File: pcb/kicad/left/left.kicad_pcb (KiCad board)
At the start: 2 copper layers, 135.9 x 89.5 mm, 61 parts, among them J1 USB_C_Receptacle_USB2.0, J2 AudioJack4, J3 Conn_01x12_Male, SW1 BOOT, SW10 SW_Push, SW12 SW_Push, SW13 SW_Push, SW14 SW_Push, SW15 SW_Push, SW17 SW_Push, SW18 SW_Push, SW19 SW_Push, SW2 RESET, SW21 SW_Push, SW22 SW_Push, SW23 SW_Push, SW24 SW_Push, SW3 SW_Push, SW31 SW_Push, SW32 SW_Push, SW33 SW_Push, SW34 SW_Push, SW4 SW_Push, SW5 SW_Push, SW7 SW_Push, SW8 SW_Push, SW9 SW_Push, U1 STM32, U2 LDO

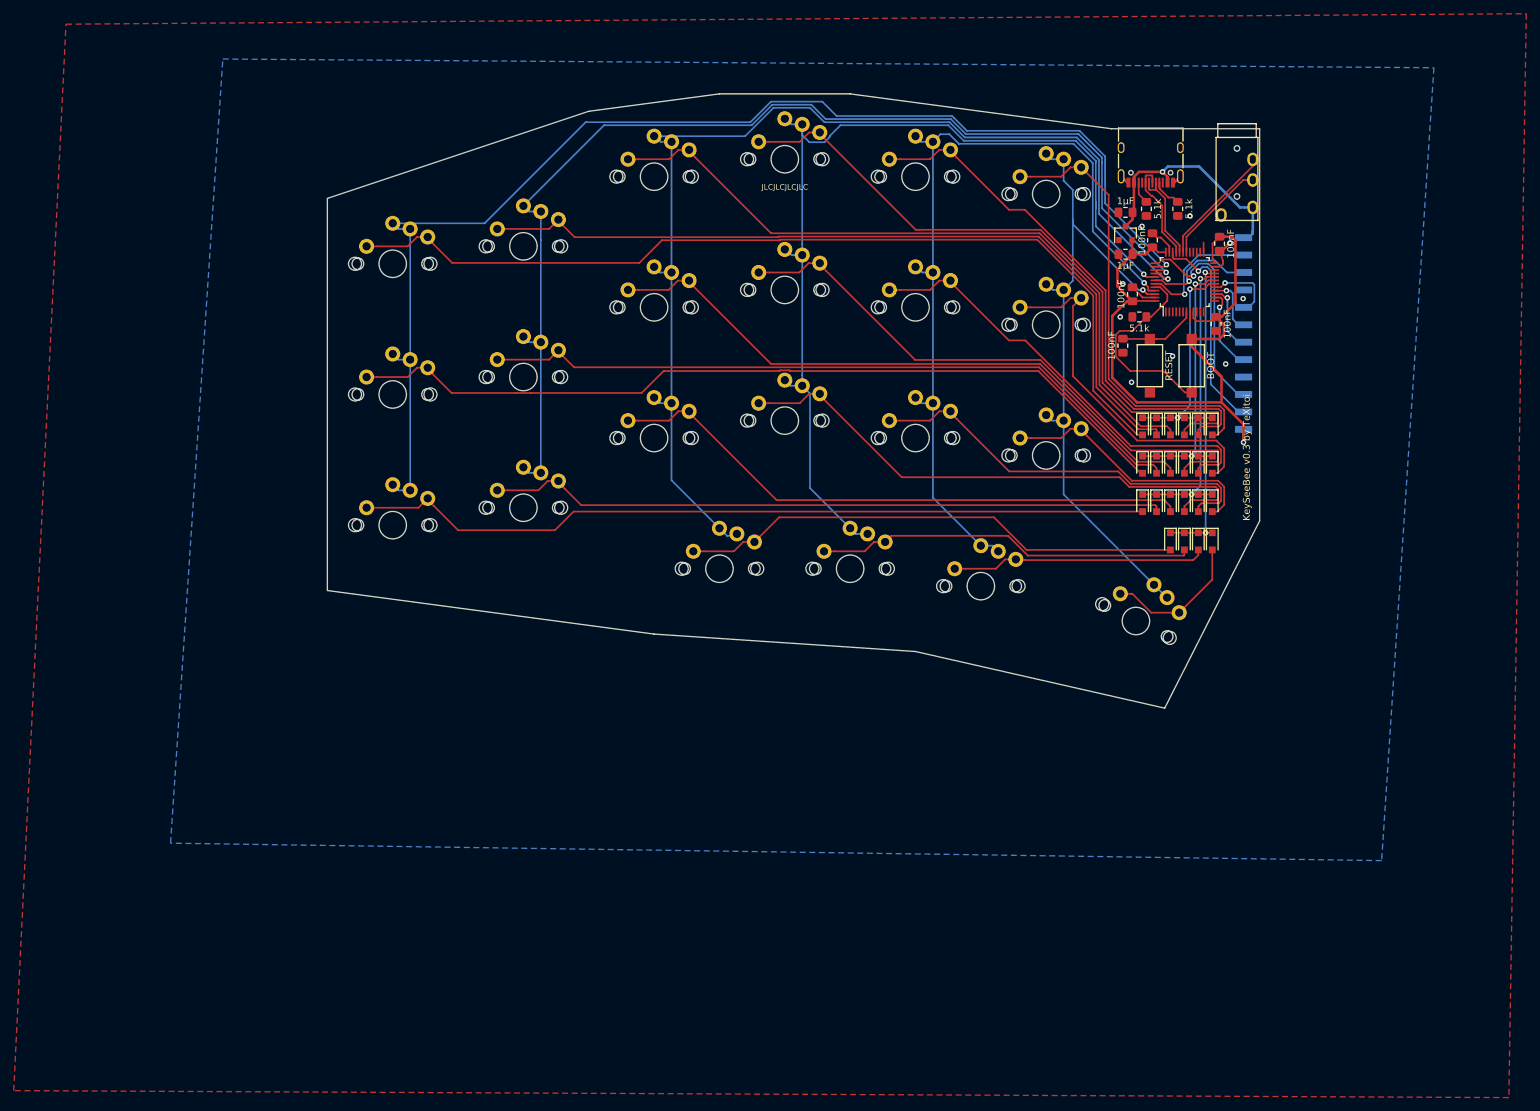
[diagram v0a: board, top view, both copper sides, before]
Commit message: Re-design the layout
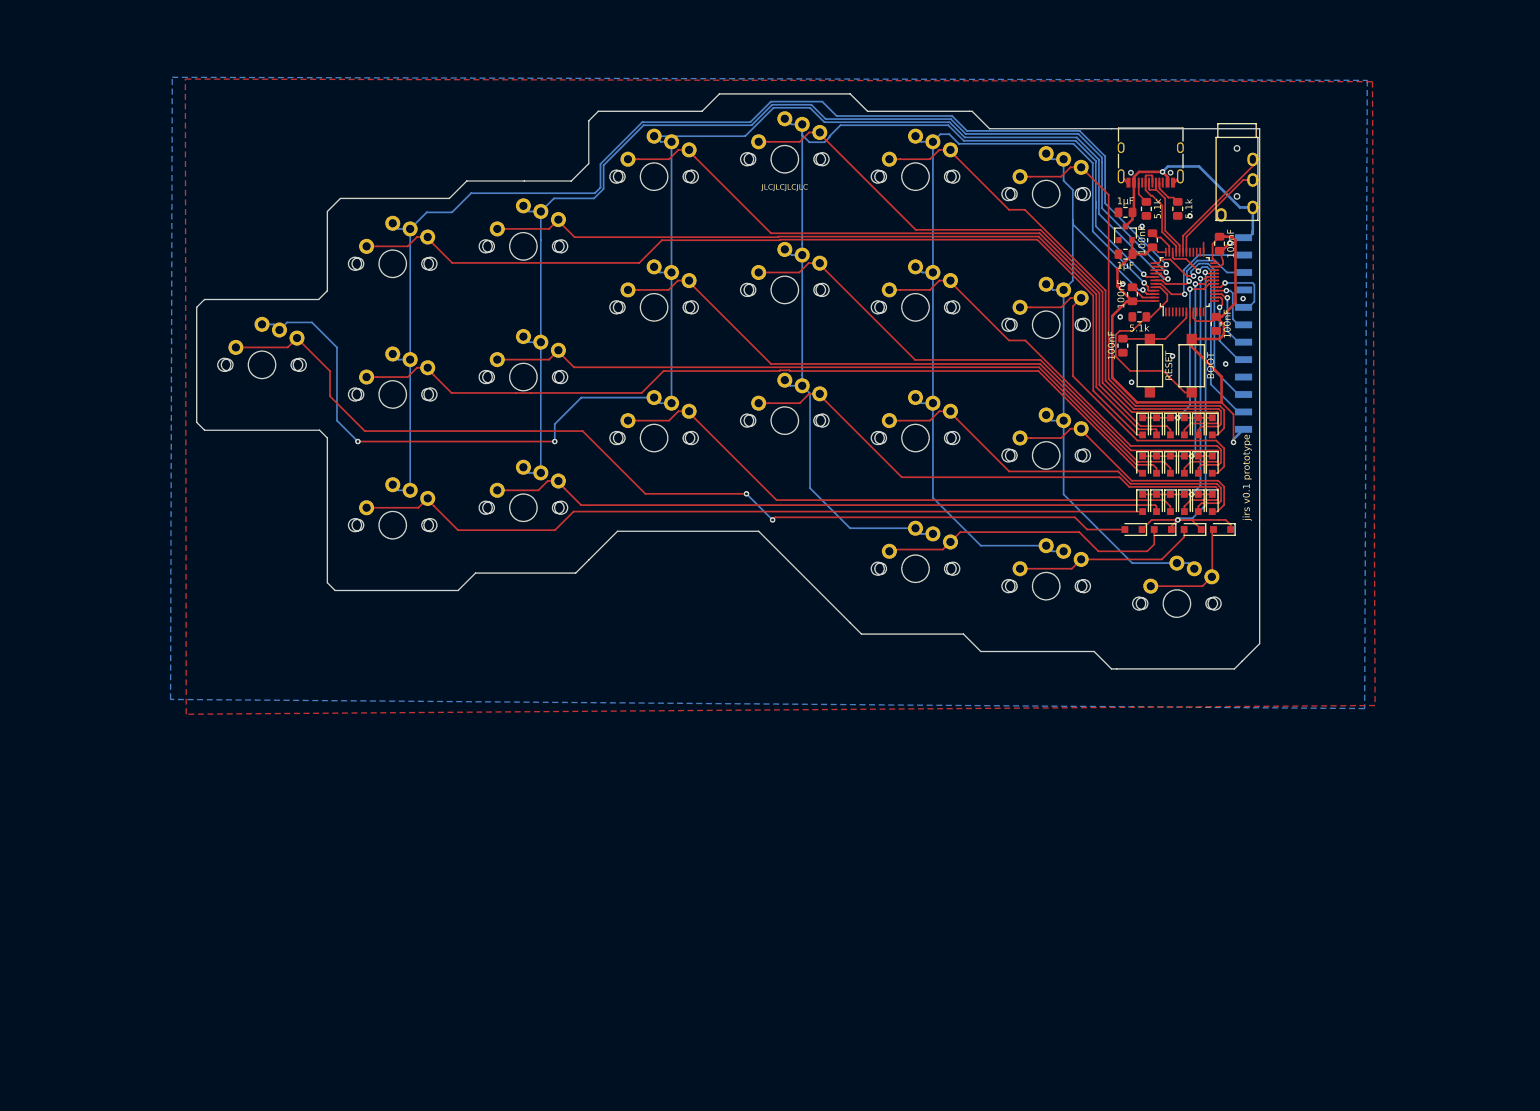
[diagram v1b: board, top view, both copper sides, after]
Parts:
- moved SW10 73.0 mm to (95.2, 81.4)
- moved SW24 9.53 mm to (190.5, 111.1)
- moved SW34 9.53 mm to (209.6, 113.7)
- moved SW15 6.49 mm to (228.6, 116.2), turned to 0 degrees
- moved D12 5.66 mm to (222.3, 105.4), turned to 180 degrees
- moved D26 3.59 mm to (226.5, 105.4), turned to 180 degrees
- moved D17 2.24 mm to (235.2, 105.4), turned to 180 degrees
- moved D36 1.91 mm to (230.9, 105.4), turned to 180 degrees
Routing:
- net Net-(D12-Pad2): track 73.7 -> 144.3 mm, vias 0 -> 2
- net COL3: track 164.9 -> 216.2 mm, vias 1 -> 3
- net ROW4: track 45.5 -> 61.0 mm
- net Net-(D26-Pad2): track 55.6 -> 43.7 mm
- net Net-(D36-Pad2): track 37.2 -> 26.9 mm
- net COL5: track 122.1 -> 131.6 mm
- net COL4: track 143.4 -> 153.0 mm
- net Net-(D17-Pad2): track 20.9 -> 16.8 mm
- net COL6: track 96.7 -> 99.0 mm
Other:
- board size 135.9 x 89.5 mm -> 154.9 x 83.8 mm
- board text added: "jirs v0.1 prototype"
- board text removed: "KeySeeBee v0.3 by TeXitoi"
